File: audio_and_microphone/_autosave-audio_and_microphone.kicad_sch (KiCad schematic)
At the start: 14 parts, among them U6 ${SIM.PARAMS}

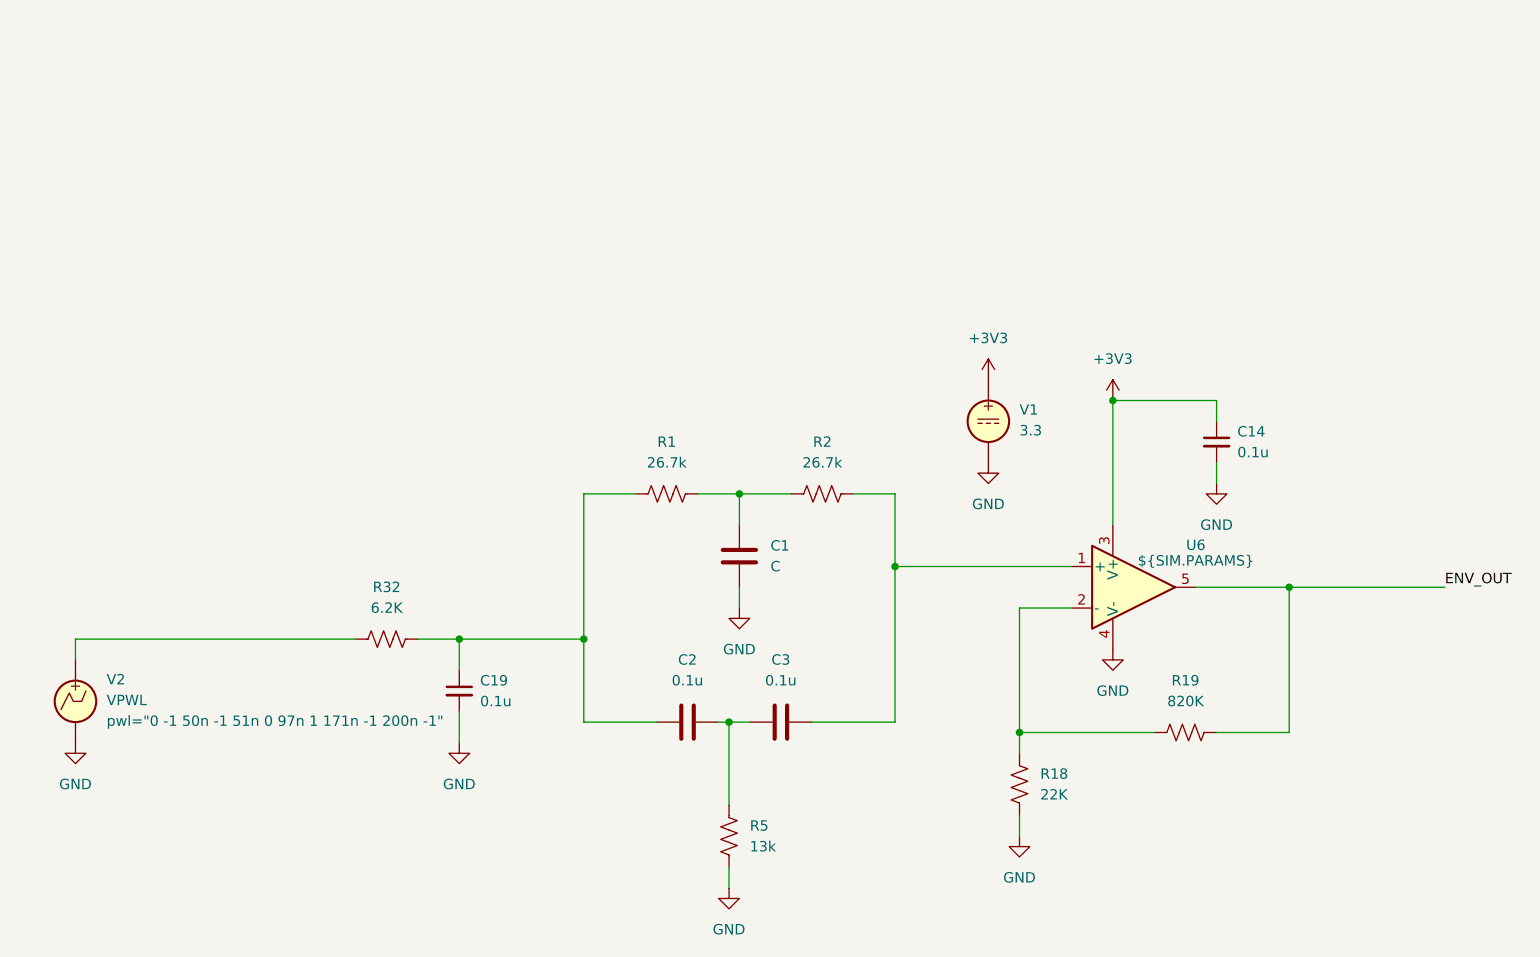
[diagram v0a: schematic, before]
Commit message: excluded voltage sources from board and replaced with connectors
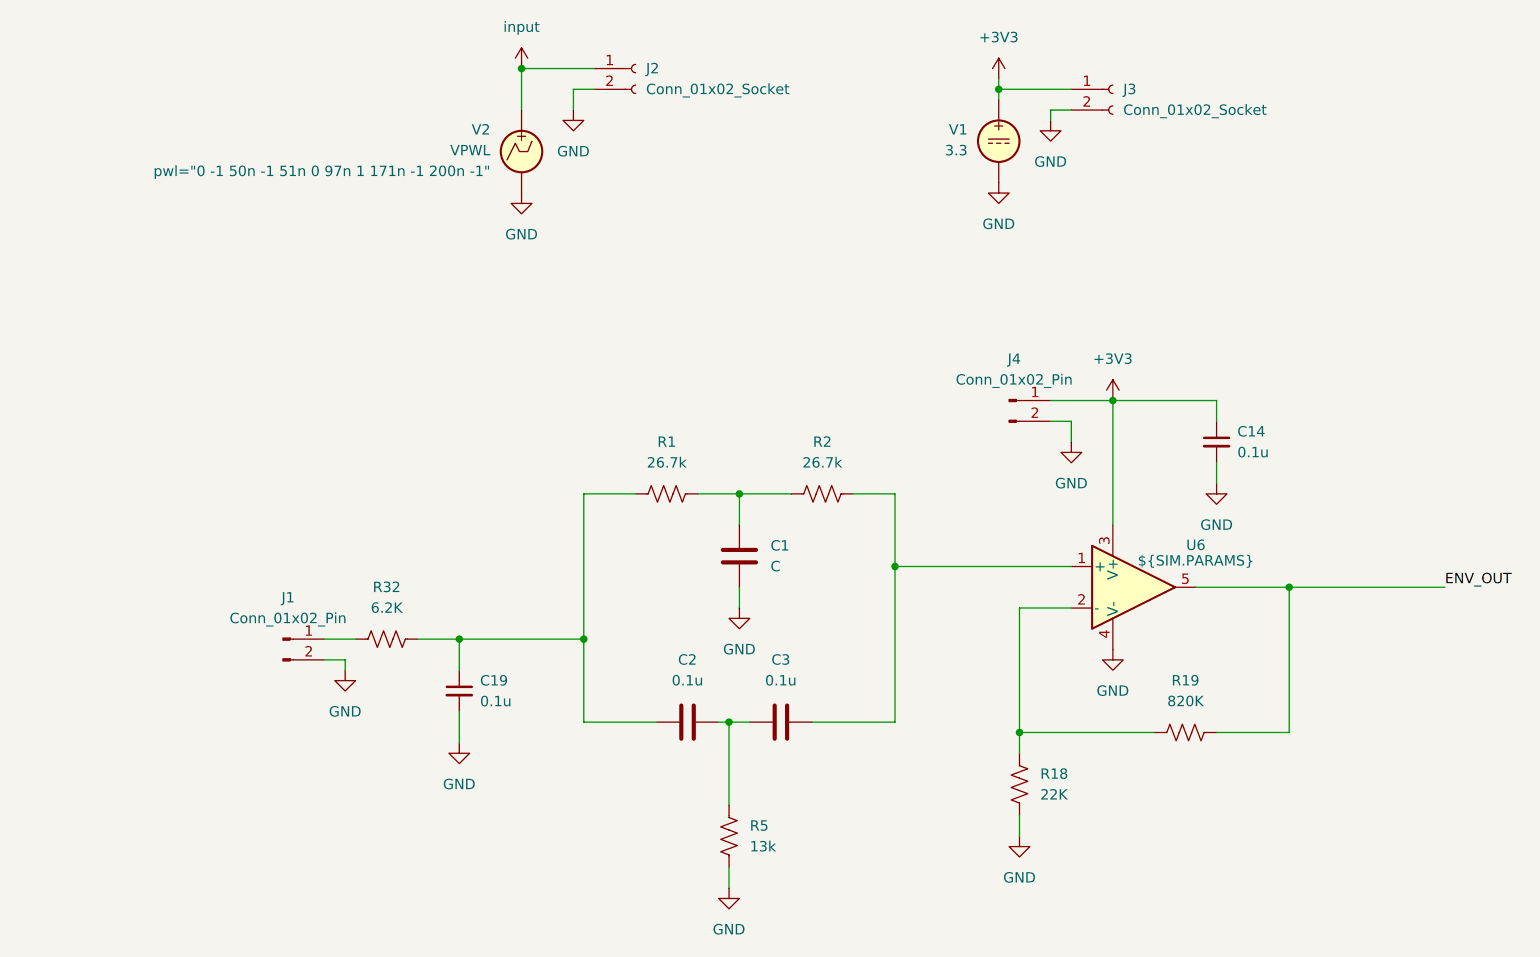
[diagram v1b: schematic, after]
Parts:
- added J1, J4: Conn_01x02_Pin, Connector_JST:JST_XA_B02B-XASK-1-A_1x02_P2.50mm_Vertical, symbol Connector:Conn_01x02_Pin
- added J2, J3: Conn_01x02_Socket, symbol Connector:Conn_01x02_Socket
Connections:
- net +3V3: now also J3.1 (Pin_1), J4.1 (Pin_1)
- net GND: now also J1.2 (Pin_2), J2.2 (Pin_2), J3.2 (Pin_2), J4.2 (Pin_2)
- net at R32.2: now also J1.1 (Pin_1); no longer V2.1
- new net input: J2.1 (Pin_1), V2.1
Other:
- moved on the sheet: V1, V2
